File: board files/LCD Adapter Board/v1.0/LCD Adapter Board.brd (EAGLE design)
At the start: 105 x 59 mm, 3 parts

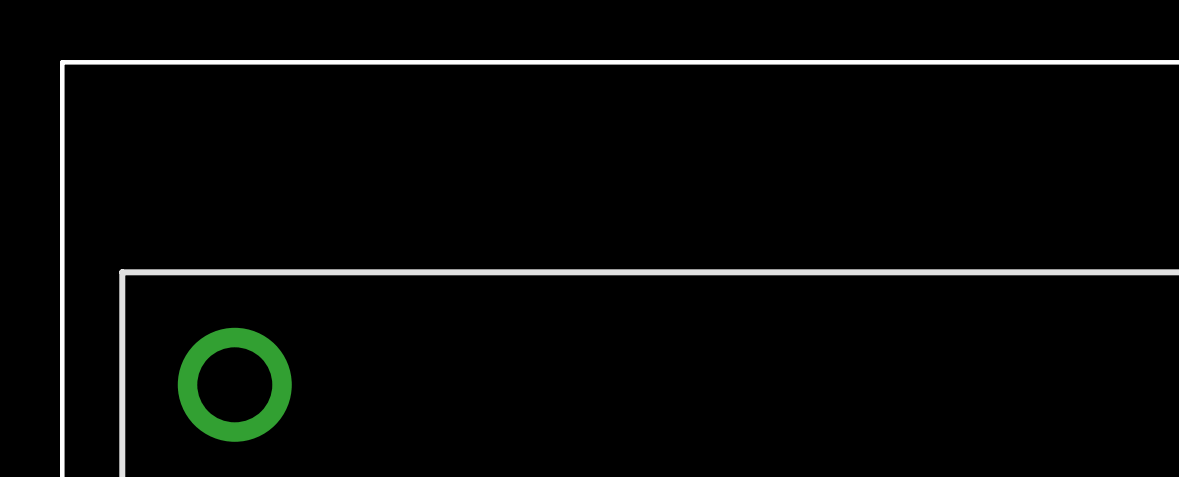
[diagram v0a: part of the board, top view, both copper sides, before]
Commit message: add boost converter
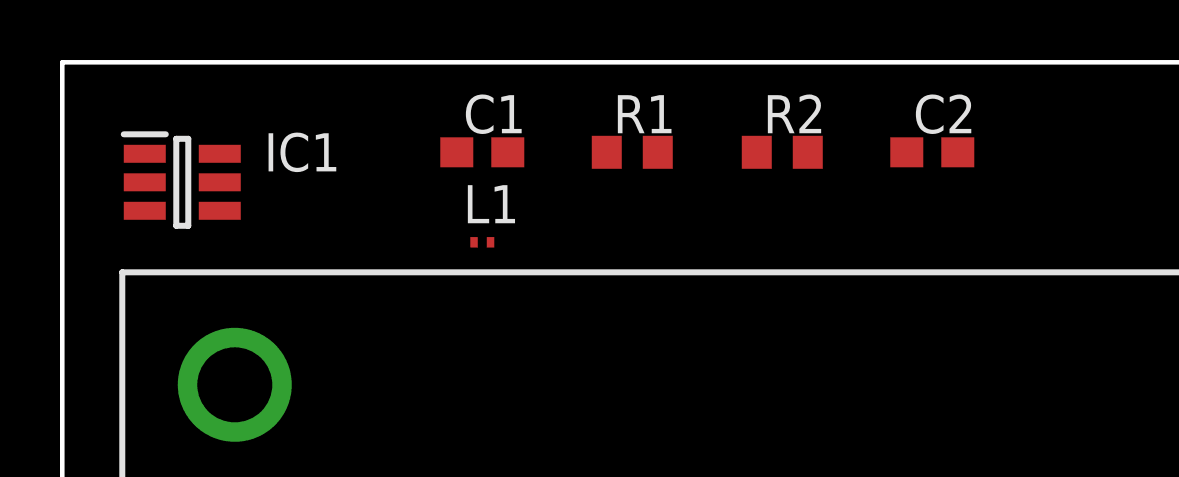
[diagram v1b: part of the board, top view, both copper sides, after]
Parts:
- added C1, C2: (no value), rcl:C0603
- added IC1: MCP1640BT-I_CHY, SamacSys_Parts:SOT95P270X145-6N
- added L1: (no value), rcl:L0201
- added R1, R2: (no value), rcl:R0603
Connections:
- removed net N$3: DS1.3
- removed net N$4: DS1.4
- new net N$17: IC1.1, L1.1
- new net N$19: IC1.4, R1.1, R2.2
- new net V_BOOST: C2.1, DS1.4, IC1.5, R1.2
- net GND: now also C1.2, C2.2, DS1.3, IC1.2, R2.1
- net VOUT_REG: now also C1.1, IC1.3, IC1.6, L1.2
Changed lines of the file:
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@@
 <attribute name="VALUE" x="88.65" y="-0.445" size="1.27" layer="27"/>
+</element>
+<element name="IC1" library="SamacSys_Parts" package="SOT95P270X145-6N" value="MCP1640BT-I_CHY" x="4" y="55" smashed="yes">
+<attribute name="ALLIED_NUMBER" value="70047503" x="4" y="55" size="1.778" layer="27" display="off"/>
+<attribute name="ALLIED_PRICE-STOCK" value="http://www.alliedelec.com/microchip-technology-inc-mcp1640bt-i-chy/70047503/" x="4" y="55" size="1.778" layer="27" display="off"/>
+<attribute name="DESCRIPTION" value="Microchip MCP1640BT-I/CHY, Boost Converter, Step Up 0.35A Adjustable, 2  5.5 V, 575 kHz, 6-pin SOT-23" x="4" y="55" size="1.778" layer="27" display="off"/>
+<attribute name="HEIGHT" value="1.45mm" x="4" y="55" size="1.778" layer="27" display="off"/>
+<attribute name="MANUFACTURER_NAME" value="Microchip" x="4" y="55" size="1.778" layer="27" display="off"/>
+<attribute name="MANUFACTURER_PART_NUMBER" value="MCP1640BT-I/CHY" x="4" y="55" size="1.778" layer="27" display="off"/>
+<attribute name="MOUSER_PART_NUMBER" value="579-MCP1640BT-I/CHY" x="4" y="55" size="1.778" layer="27" display="off"/>
+<attribute name="MOUSER_PRICE-STOCK" value="https://www.mouser.com/Search/Refine.aspx?Keyword=579-MCP1640BT-I%2FCHY" x="4" y="55" size="1.778" layer="27" display="off"/>
+<attribute name="NAME" x="8" y="56" size="1.27" layer="25" align="center"/>
+<attribute name="RS_PART_NUMBER" value="7386250P" x="4" y="55" size="1.778" layer="27" display="off"/>
+<attribute name="RS_PRICE-STOCK" value="http://uk.rs-online.com/web/p/products/7386250P" x="4" y="55" size="1.778" layer="27" display="off"/>
+</element>
+<element name="C1" library="rcl" library_urn="urn:adsk.eagle:library:334" package="C0603" package3d_urn="urn:adsk.eagle:package:23616/2" value="" x="14" y="56" smashed="yes">
+<attribute name="NAME" x="13.365" y="56.635" size="1.27" layer="25"/>
+<attribute name="POPULARITY" value="73" x="14" y="56" size="1.778" layer="27" display="off"/>
+<attribute name="SPICEPREFIX" value="C" x="14" y="56" size="1.778" layer="27" display="off"/>
+<attribute name="VALUE" x="13.365" y="54.095" size="1.27" layer="27"/>
+</element>
+<element name="L1" library="rcl" library_urn="urn:adsk.eagle:library:334" package="L0201" package3d_urn="urn:adsk.eagle:package:23513/2" value="" x="14" y="53" smashed="yes">
+<attribute name="NAME" x="13.365" y="53.635" size="1.27" layer="25"/>
+<attribute name="POPULARITY" value="0" x="14" y="53" size="1.778" layer="27" display="off"/>
+<attribute name="SPICEPREFIX" value="L" x="14" y="53" size="1.778" layer="27" display="off"/>
+<attribute name="VALUE" x="13.365" y="51.095" size="1.27" layer="27"/>
+</element>
+<element name="R1" library="rcl" library_urn="urn:adsk.eagle:library:334" package="R0603" package3d_urn="urn:adsk.eagle:package:23555/3" value="" x="19" y="56" smashed="yes">
+<attribute name="NAME" x="18.365" y="56.635" size="1.27" layer="25"/>
+<attribute name="POPULARITY" value="70" x="19" y="56" size="1.778" layer="27" display="off"/>
+<attribute name="SPICEPREFIX" value="R" x="19" y="56" size="1.778" layer="27" display="off"/>
+<attribute name="VALUE" x="18.365" y="54.095" size="1.27" layer="27"/>
+</element>
+<element name="R2" library="rcl" library_urn="urn:adsk.eagle:library:334" package="R0603" package3d_urn="urn:adsk.eagle:package:23555/3" value="" x="24" y="56" smashed="yes">
+<attribute name="NAME" x="23.365" y="56.635" size="1.27" layer="25"/>
+<attribute name="POPULARITY" value="70" x="24" y="56" size="1.778" layer="27" display="off"/>
+<attribute name="SPICEPREFIX" value="R" x="24" y="56" size="1.778" layer="27" display="off"/>
+<attribute name="VALUE" x="23.365" y="54.095" size="1.27" layer="27"/>
+</element>
+<element name="C2" library="rcl" library_urn="urn:adsk.eagle:library:334" package="C0603" package3d_urn="urn:adsk.eagle:package:23616/2" value="" x="29" y="56" smashed="yes">
+<attribute name="NAME" x="28.365" y="56.635" size="1.27" layer="25"/>
+<attribute name="POPULARITY" value="73" x="29" y="56" size="1.778" layer="27" display="off"/>
+<attribute name="SPICEPREFIX" value="C" x="29" y="56" size="1.778" layer="27" display="off"/>
+<attribute name="VALUE" x="28.365" y="54.095" size="1.27" layer="27"/>
 </element>
 </elements>
@@
 <signal name="N$2">
 <contactref element="DS1" pad="2"/>
-</signal>
-<signal name="N$3">
-<contactref element="DS1" pad="3"/>
-</signal>
-<signal name="N$4">
-<contactref element="DS1" pad="4"/>
 </signal>
 <signal name="N$5">
@@
 <contactref element="PORTC" pad="2"/>
 <contactref element="PORTA" pad="2"/>
-<wire x1="89.92" y1="55.27" x2="89.92" y2="5.27" width="0" layer="19" extent="1-1"/>
+<contactref element="C1" pad="2"/>
+<contactref element="IC1" pad="2"/>
+<contactref element="R2" pad="1"/>
+<contactref element="C2" pad="2"/>
+<contactref element="DS1" pad="3"/>
+<wire x1="89.92" y1="5.27" x2="89.92" y2="55.27" width="0" layer="19" extent="1-1"/>
+<wire x1="45.02" y1="11.75" x2="89.92" y2="5.27" width="0" layer="19" extent="1-1"/>
+<wire x1="29.85" y1="56" x2="45.02" y2="11.75" width="0" layer="19" extent="1-1"/>
+<wire x1="23.15" y1="56" x2="29.85" y2="56" width="0" layer="19" extent="1-1"/>
+<wire x1="14.85" y1="56" x2="23.15" y2="56" width="0" layer="19" extent="1-1"/>
+<wire x1="2.75" y1="55" x2="14.85" y2="56" width="0" layer="19" extent="1-1"/>
 </signal>
 <signal name="ENABLE">
@@
 <contactref element="PORTC" pad="1"/>
 <contactref element="PORTA" pad="1"/>
-<wire x1="89.92" y1="52.73" x2="89.92" y2="2.73" width="0" layer="19" extent="1-1"/>
+<contactref element="IC1" pad="6"/>
+<contactref element="C1" pad="1"/>
+<contactref element="IC1" pad="3"/>
+<contactref element="L1" pad="2"/>
+<wire x1="89.92" y1="2.73" x2="89.92" y2="52.73" width="0" layer="19" extent="1-1"/>
+<wire x1="5.25" y1="55.95" x2="89.92" y2="2.73" width="0" layer="19" extent="1-1"/>
+<wire x1="2.75" y1="54.05" x2="5.25" y2="55.95" width="0" layer="19" extent="1-1"/>
+<wire x1="13.15" y1="56" x2="2.75" y2="54.05" width="0" layer="19" extent="1-1"/>
+<wire x1="14.275" y1="53" x2="13.15" y2="56" width="0" layer="19" extent="1-1"/>
 </signal>
 <signal name="N$15">
@@
 <contactref element="DS1" pad="16"/>
 </signal>
+<signal name="N$17">
+<contactref element="IC1" pad="1"/>
+<contactref element="L1" pad="1"/>
+<wire x1="2.75" y1="55.95" x2="13.725" y2="53" width="0" layer="19" extent="1-1"/>
+</signal>
+<signal name="N$19">
+<contactref element="R1" pad="1"/>
+<contactref element="R2" pad="2"/>
+<contactref element="IC1" pad="4"/>
+<wire x1="18.15" y1="56" x2="24.85" y2="56" width="0" layer="19" extent="1-1"/>
+<wire x1="5.25" y1="54.05" x2="18.15" y2="56" width="0" layer="19" extent="1-1"/>
+</signal>
+<signal name="V_BOOST">
+<contactref element="IC1" pad="5"/>
+<contactref element="R1" pad="2"/>
+<contactref element="C2" pad="1"/>
+<contactref element="DS1" pad="4"/>
+<wire x1="19.85" y1="56" x2="28.15" y2="56" width="0" layer="19" extent="1-1"/>
+<wire x1="5.25" y1="55" x2="19.85" y2="56" width="0" layer="19" extent="1-1"/>
+<wire x1="42.48" y1="11.75" x2="28.15" y2="56" width="0" layer="19" extent="1-1"/>
+</signal>
 </signals>
